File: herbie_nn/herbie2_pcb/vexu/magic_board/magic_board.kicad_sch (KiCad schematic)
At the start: 91 parts, among them J1 4P4C, J2 Conn_ARM_JTAG_SWD_10, J3 USB_C_Receptacle_USB2.0_14P, J4 Conn_01x04_Socket, J5 Conn_01x05_Pin, J6 Conn_01x05_Pin, J7 Conn_01x05_Pin, J8 Conn_01x04_Socket, Q2 MMBT3904, U11 74LVC125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

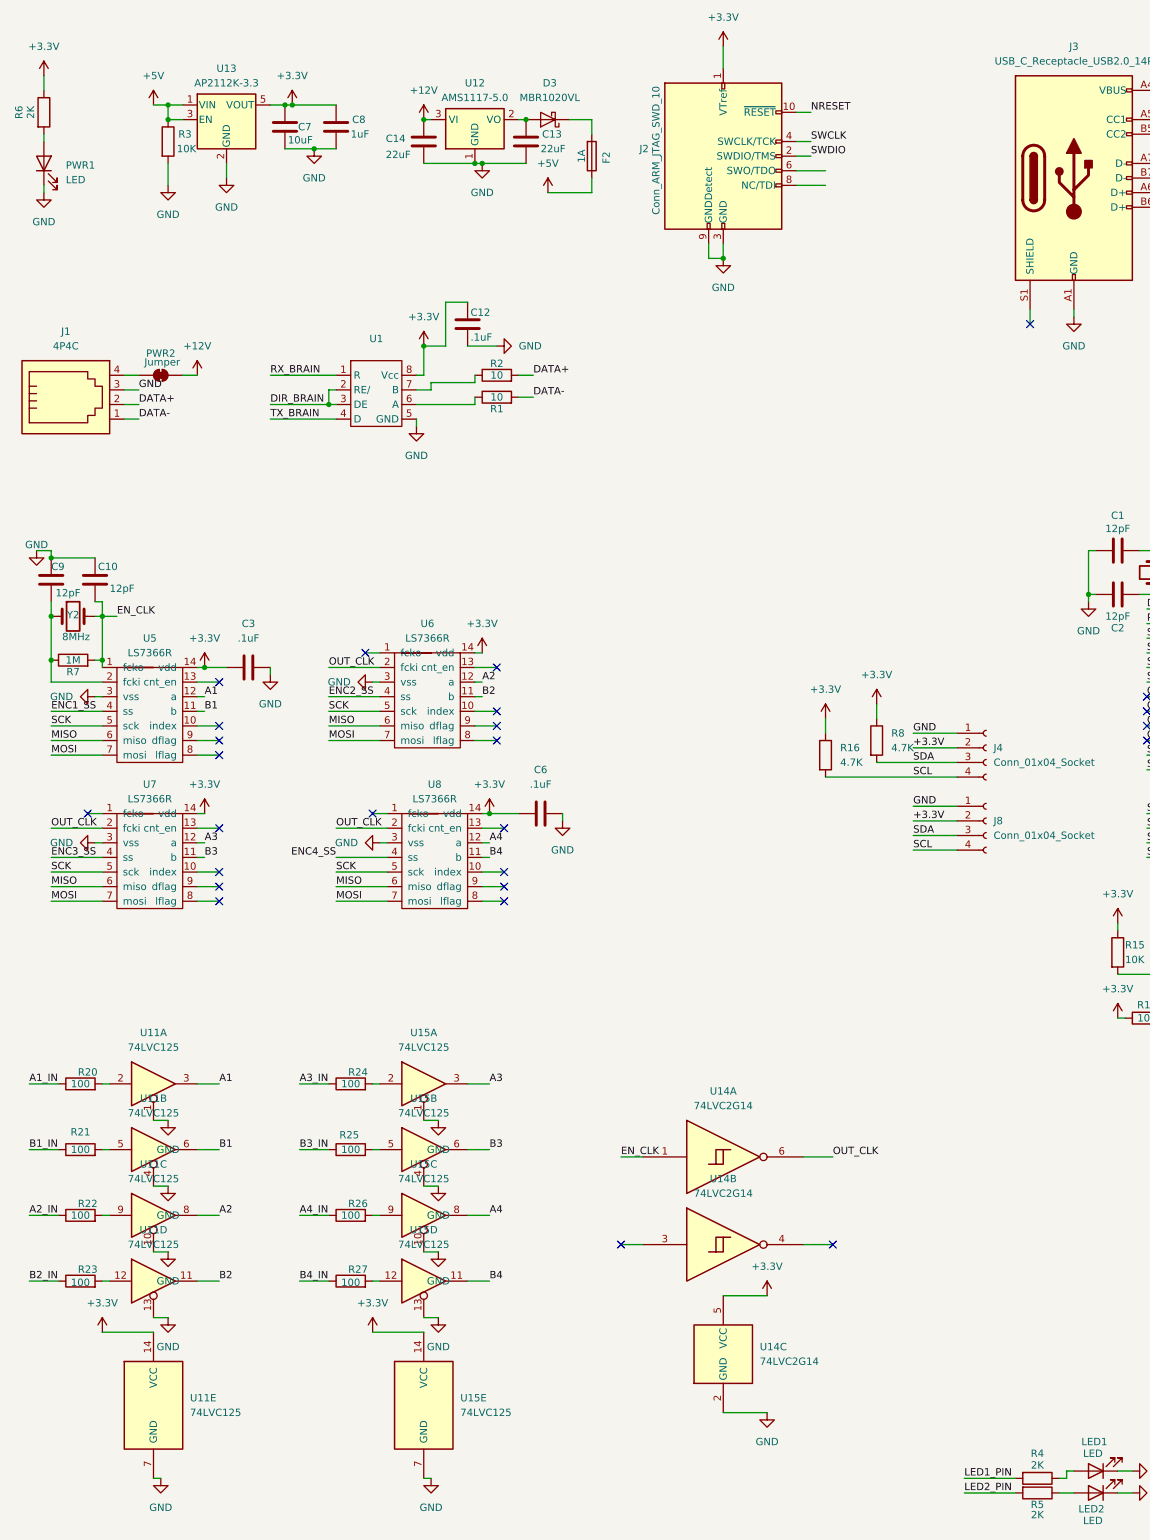
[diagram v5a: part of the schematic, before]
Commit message: changed resistors to 3K
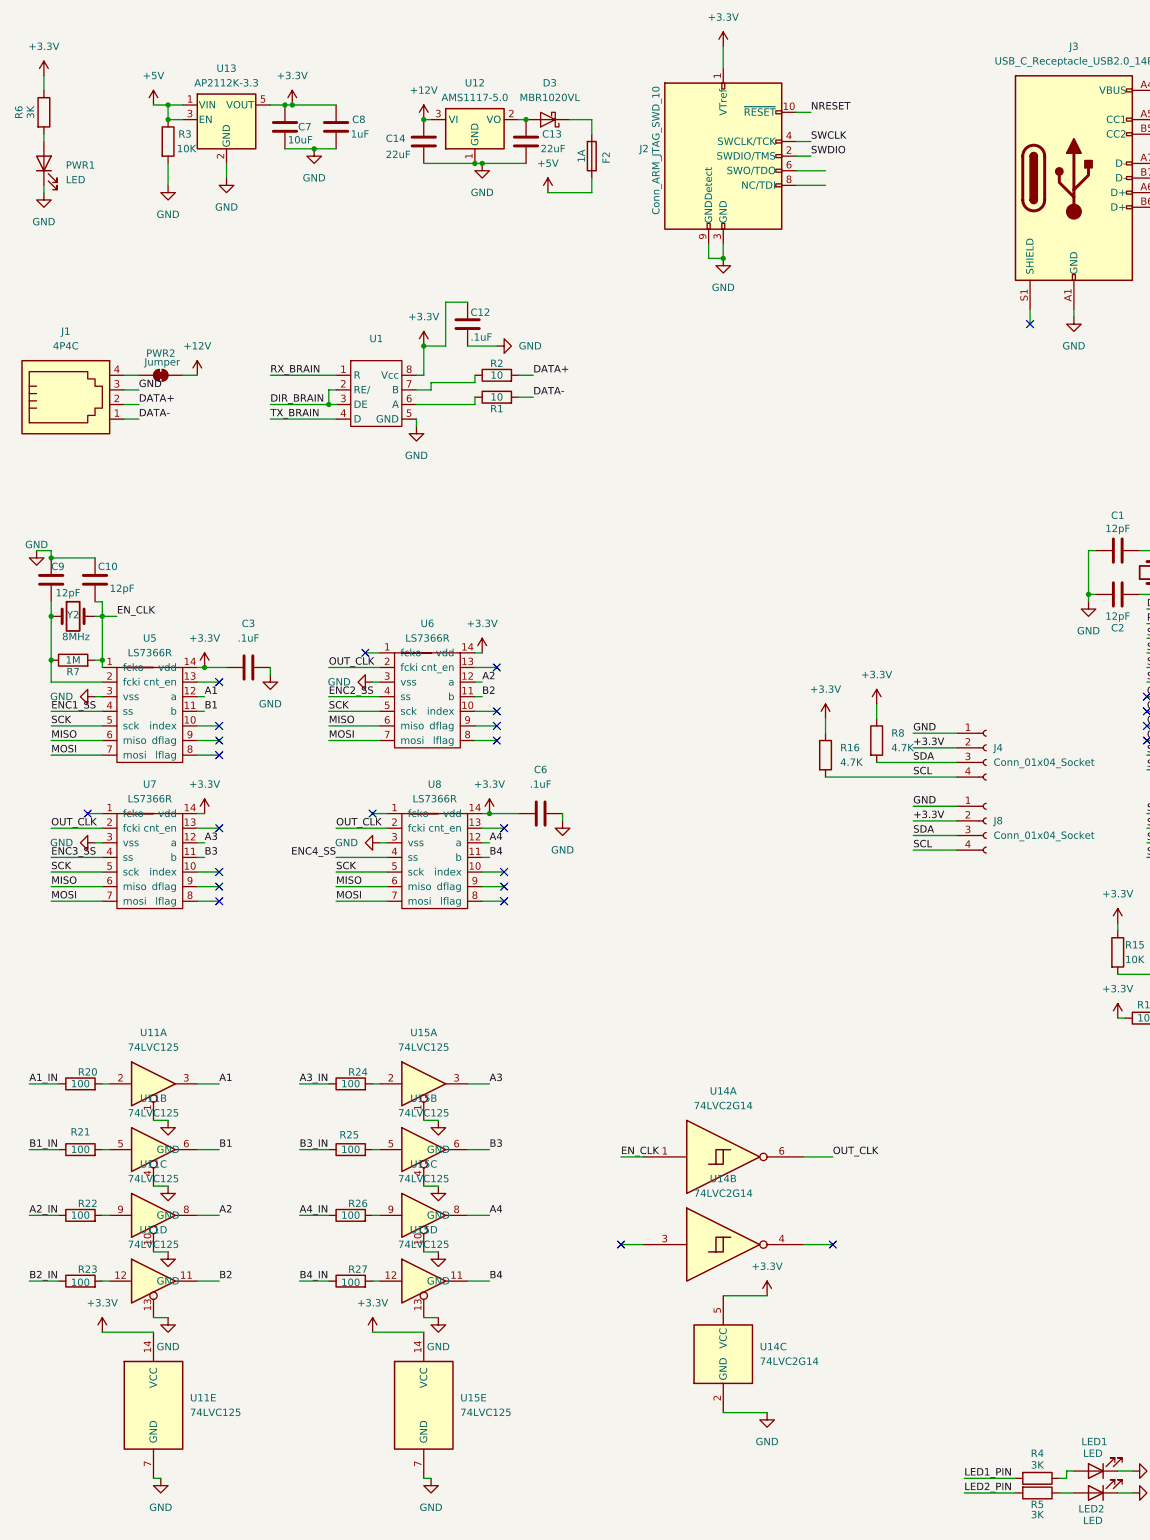
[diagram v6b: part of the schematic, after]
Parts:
- R4, R5, R6: value 2K -> 3K
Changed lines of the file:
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@@
 			)
 		)
-		(property "Value" "2K"
+		(property "Value" "3K"
 			(at 198.12 276.86 90)
 			(effects
@@
 			)
 		)
-		(property "Value" "2K"
+		(property "Value" "3K"
 			(at 198.12 268.224 90)
 			(effects
@@
 			)
 		)
-		(property "Value" "2K"
+		(property "Value" "3K"
 			(at 23.114 33.02 90)
 			(effects
